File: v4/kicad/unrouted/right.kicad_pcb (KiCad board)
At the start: 2 copper layers, 160 x 118.6 mm, 72 parts

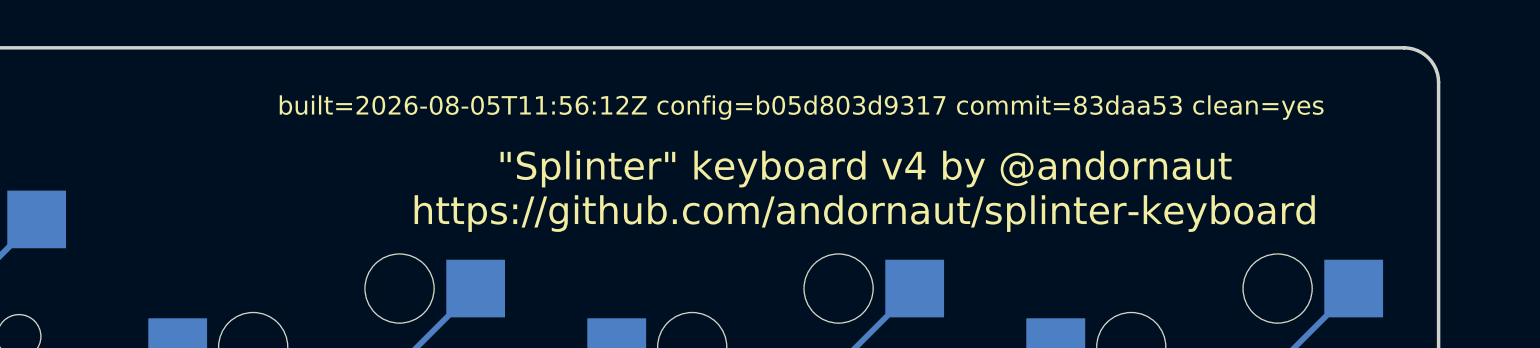
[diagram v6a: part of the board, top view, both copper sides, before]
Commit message: Restamp the boards for the new config hash
Adding the un-filleted outlines changed the config.yaml hash, which every board's
stamp carries, so all four are restamped. Copper, pads, zones and outline are
identical to the previous build: no pcbs: entry references those outlines.
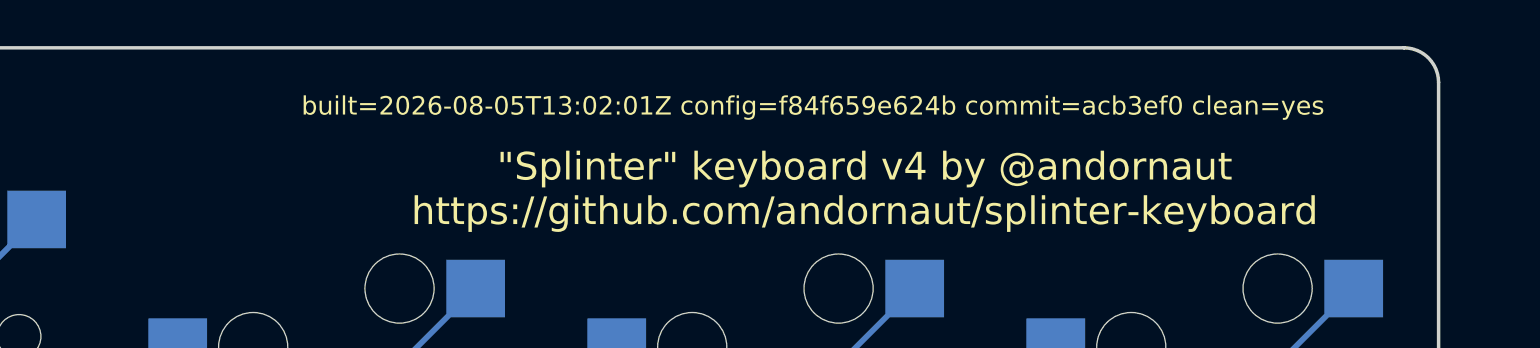
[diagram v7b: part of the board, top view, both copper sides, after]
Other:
- board text added: "built=2026-08-05T13:02:01Z config=f84f659e624b commit=acb3ef0 clean=yes"
- board text removed: "built=2026-08-05T11:56:12Z config=b05d803d9317 commit=83daa53 clean=yes"

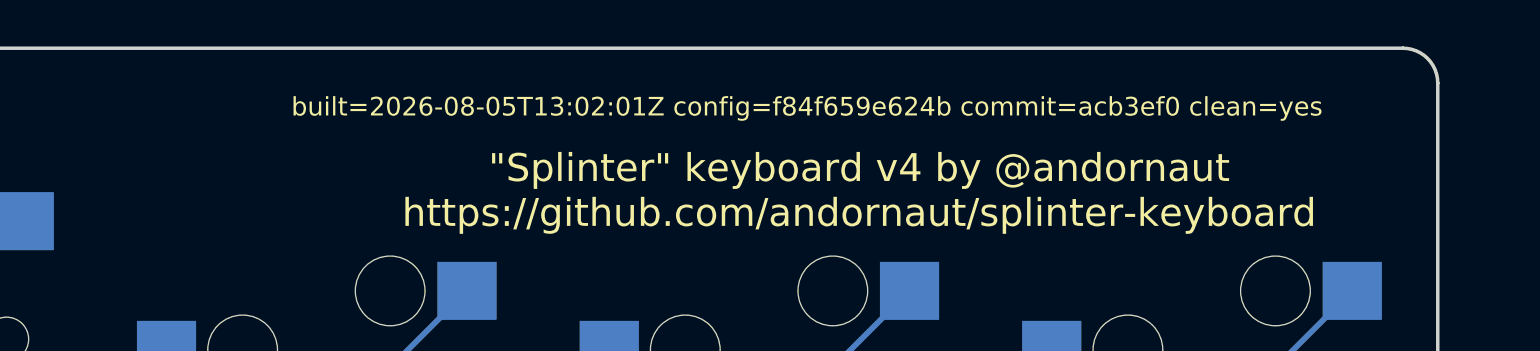
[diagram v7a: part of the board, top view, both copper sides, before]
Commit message: Restamp the boards against the reworked config comment
The stamp keys on the config hash alone, so correcting the comment above
_wallsleft_unfilleted moved every board to stale. Nothing about the design
changed: teardrops hold at 288 left and 303 right, segments at 318 and 334, and
the diff is the stamp plus regenerated UUIDs.

Built from a clean tree so commit= names the source these boards came from.
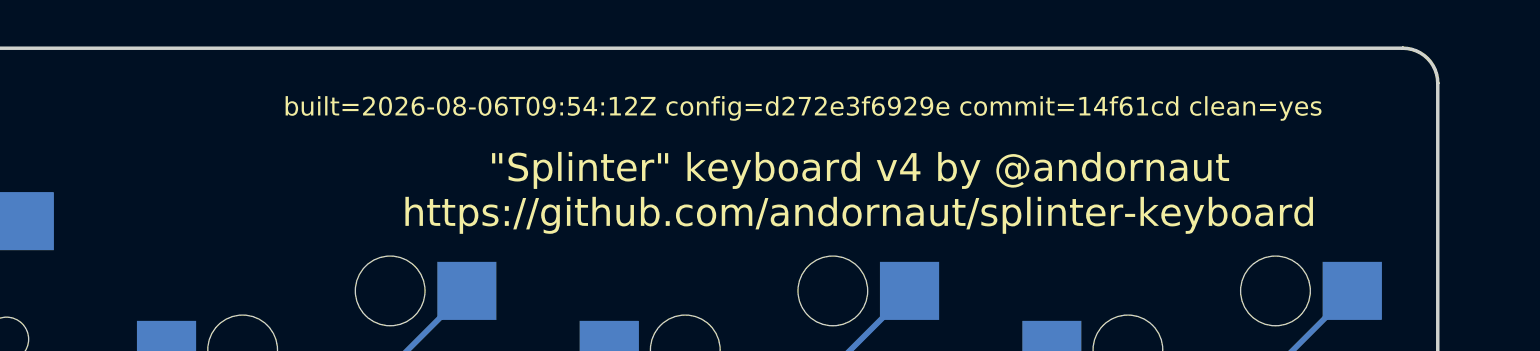
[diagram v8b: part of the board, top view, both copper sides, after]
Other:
- board text added: "built=2026-08-06T09:54:12Z config=d272e3f6929e commit=14f61cd clean=yes"
- board text removed: "built=2026-08-05T13:02:01Z config=f84f659e624b commit=acb3ef0 clean=yes"
